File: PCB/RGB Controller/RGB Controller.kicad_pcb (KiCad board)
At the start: 2 copper layers, 69.9 x 88.9 mm, 62 parts, among them J1 Conn_01x06, J10 Conn_01x04, J11 Conn_01x03, J12 641737-1, J2 Conn_01x04, J3 Conn_01x04, J4 Conn_01x04, J5 Conn_01x04, J6 Conn_01x04, J7 Conn_01x04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

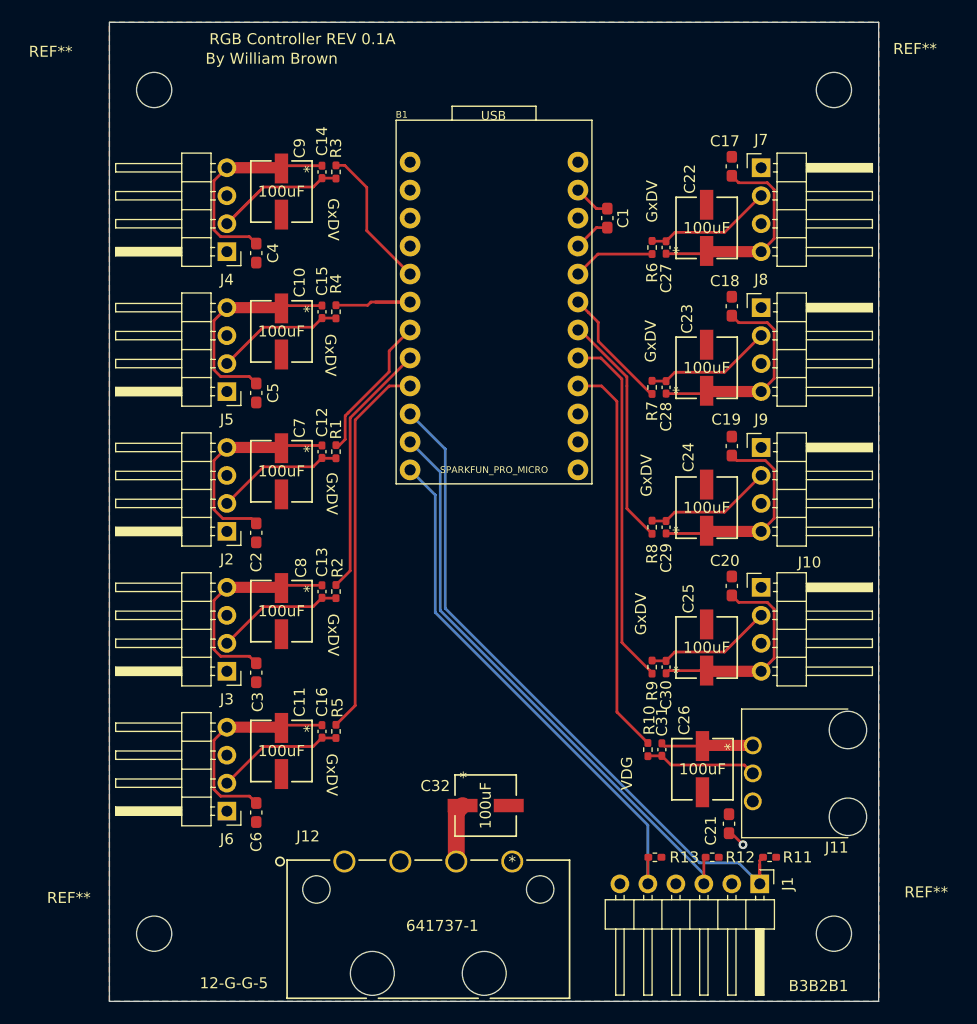
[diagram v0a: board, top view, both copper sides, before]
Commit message: Rev 0.1B hardware - Fixes Corsair Header pinout, 0.1A stencil compatible
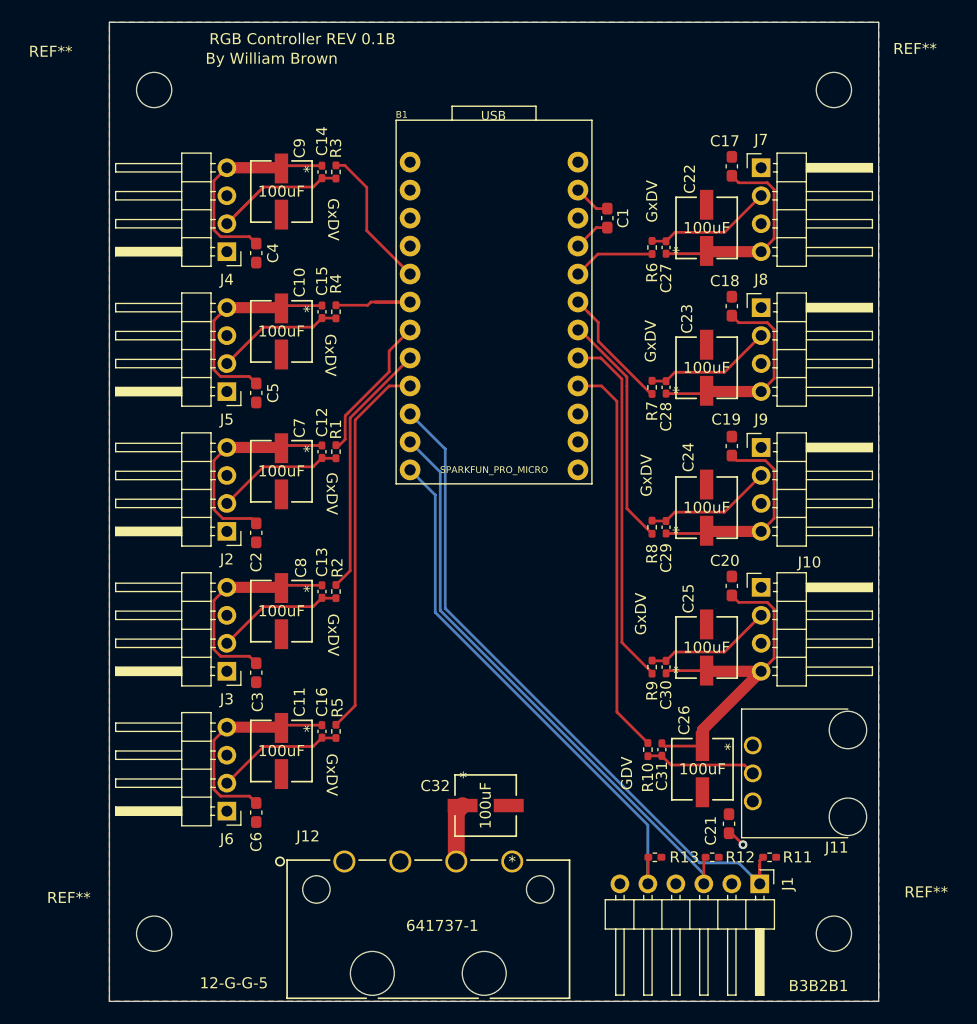
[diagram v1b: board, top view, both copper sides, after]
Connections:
- J11 pad 1: +5V -> GND
- J11 pad 3: GND -> +5V
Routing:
- net GND: track 192.1 -> 196.6 mm
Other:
- board text added: "GDV"
- board text added: "RGB Controller REV 0.1B"
- board text removed: "RGB Controller REV 0.1A"
- board text removed: "VDG"
